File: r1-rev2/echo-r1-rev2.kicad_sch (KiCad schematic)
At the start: 100 parts, among them J1 TYPE-C-31-M-12, J2 TF-115, J6 AFC07-S30ECA-00, J7 Conn_SWDUART, J9 Micro_SD_Card, Q1 AO3401A, Q2 AO3401A, Q5 AO3401A, SW1 A, SW10 SELECT, SW11 VOL+, SW12 VOL-, SW13 POWER, SW14 HOLD, SW2 B, SW3 X, SW4 Y, SW5 DPAD↑, SW6 DPAD↓, SW7 DPAD←, SW8 DPAD→, SW9 START, U1 STM32H7R3Z8Jx, U10 USBLC6-2SC6, U11 TPAZ1143-04F, U12 TPAZ1143-04F, U13 TPAZ1143-04F, U14 TPAZ1143-04F, U2 W958D8NBYA5I, Y1 SC-32S32.768kHz20PPM12.5pF, Y2 XTM32024000JT00351001

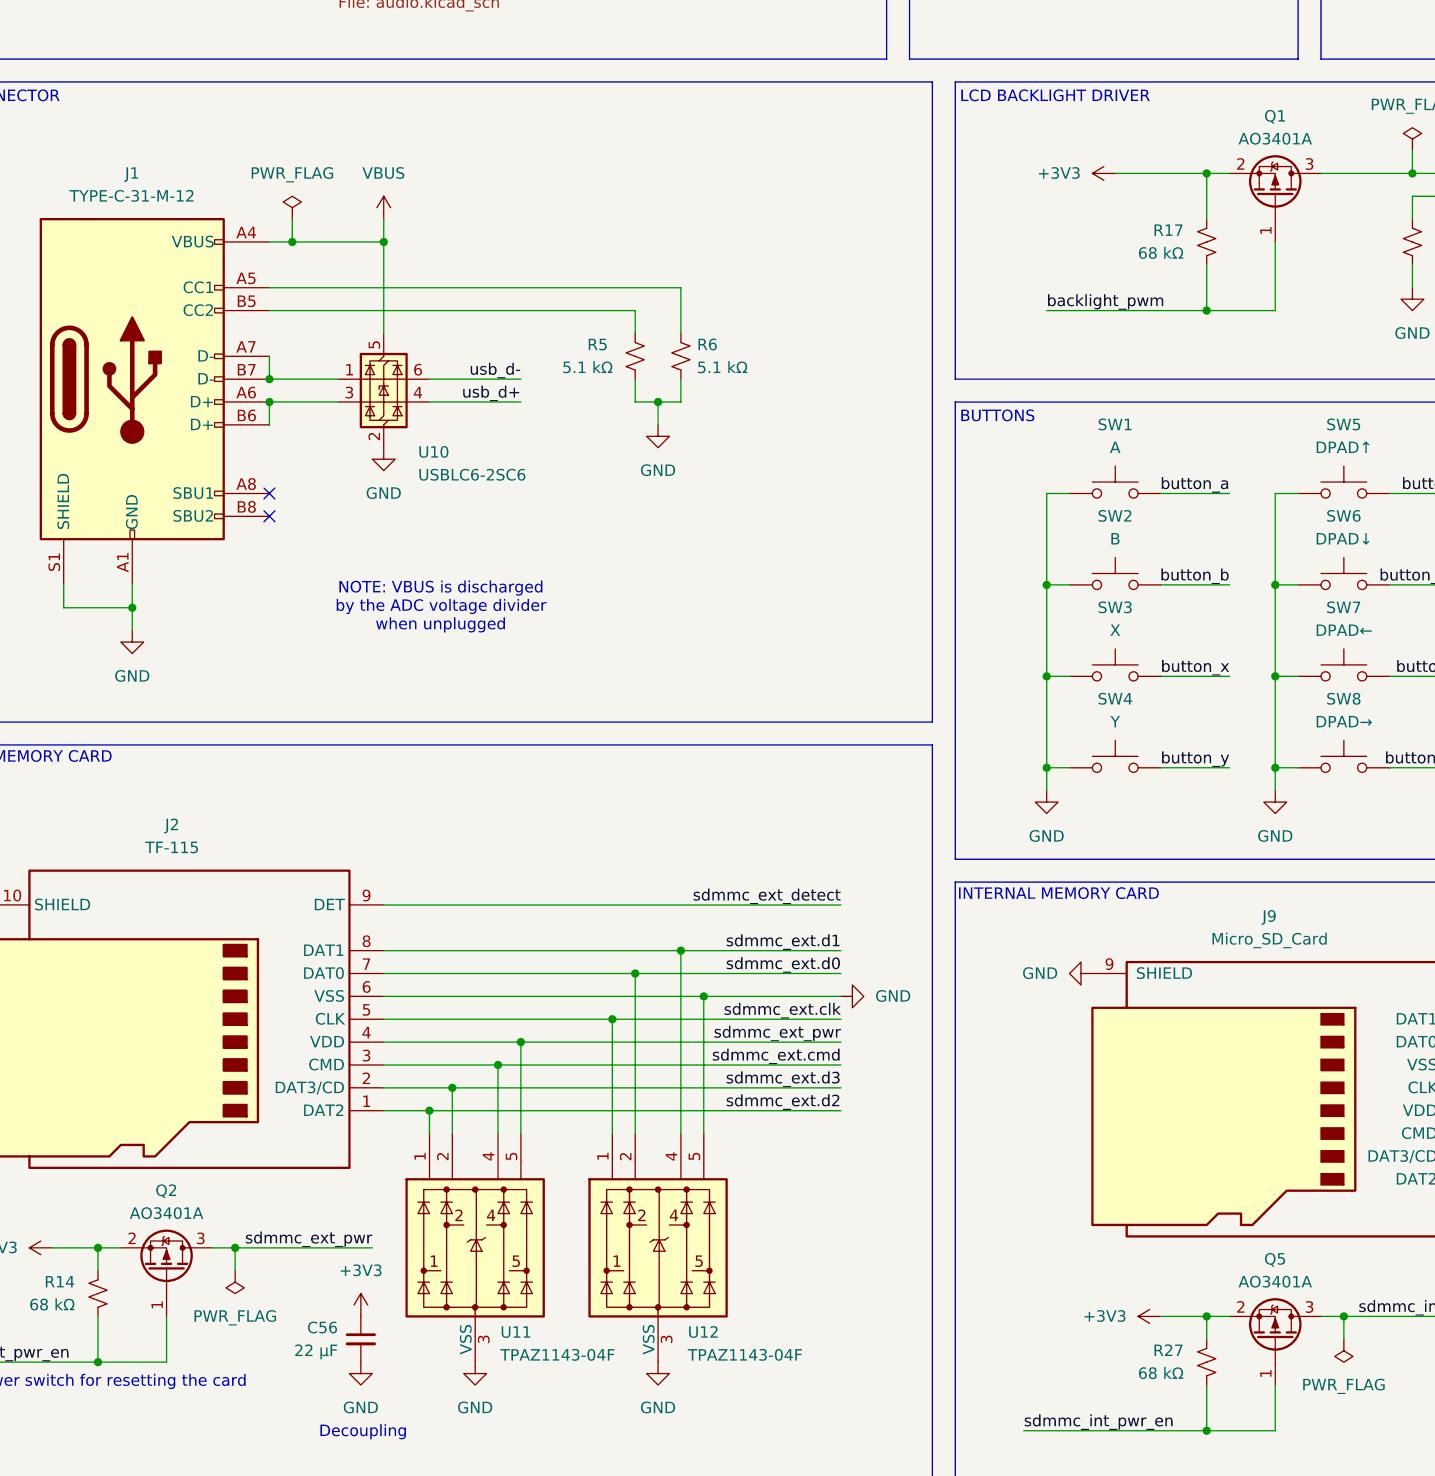
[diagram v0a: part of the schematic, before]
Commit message: Fix symbol library links & resync footprints from KiCAD libraries
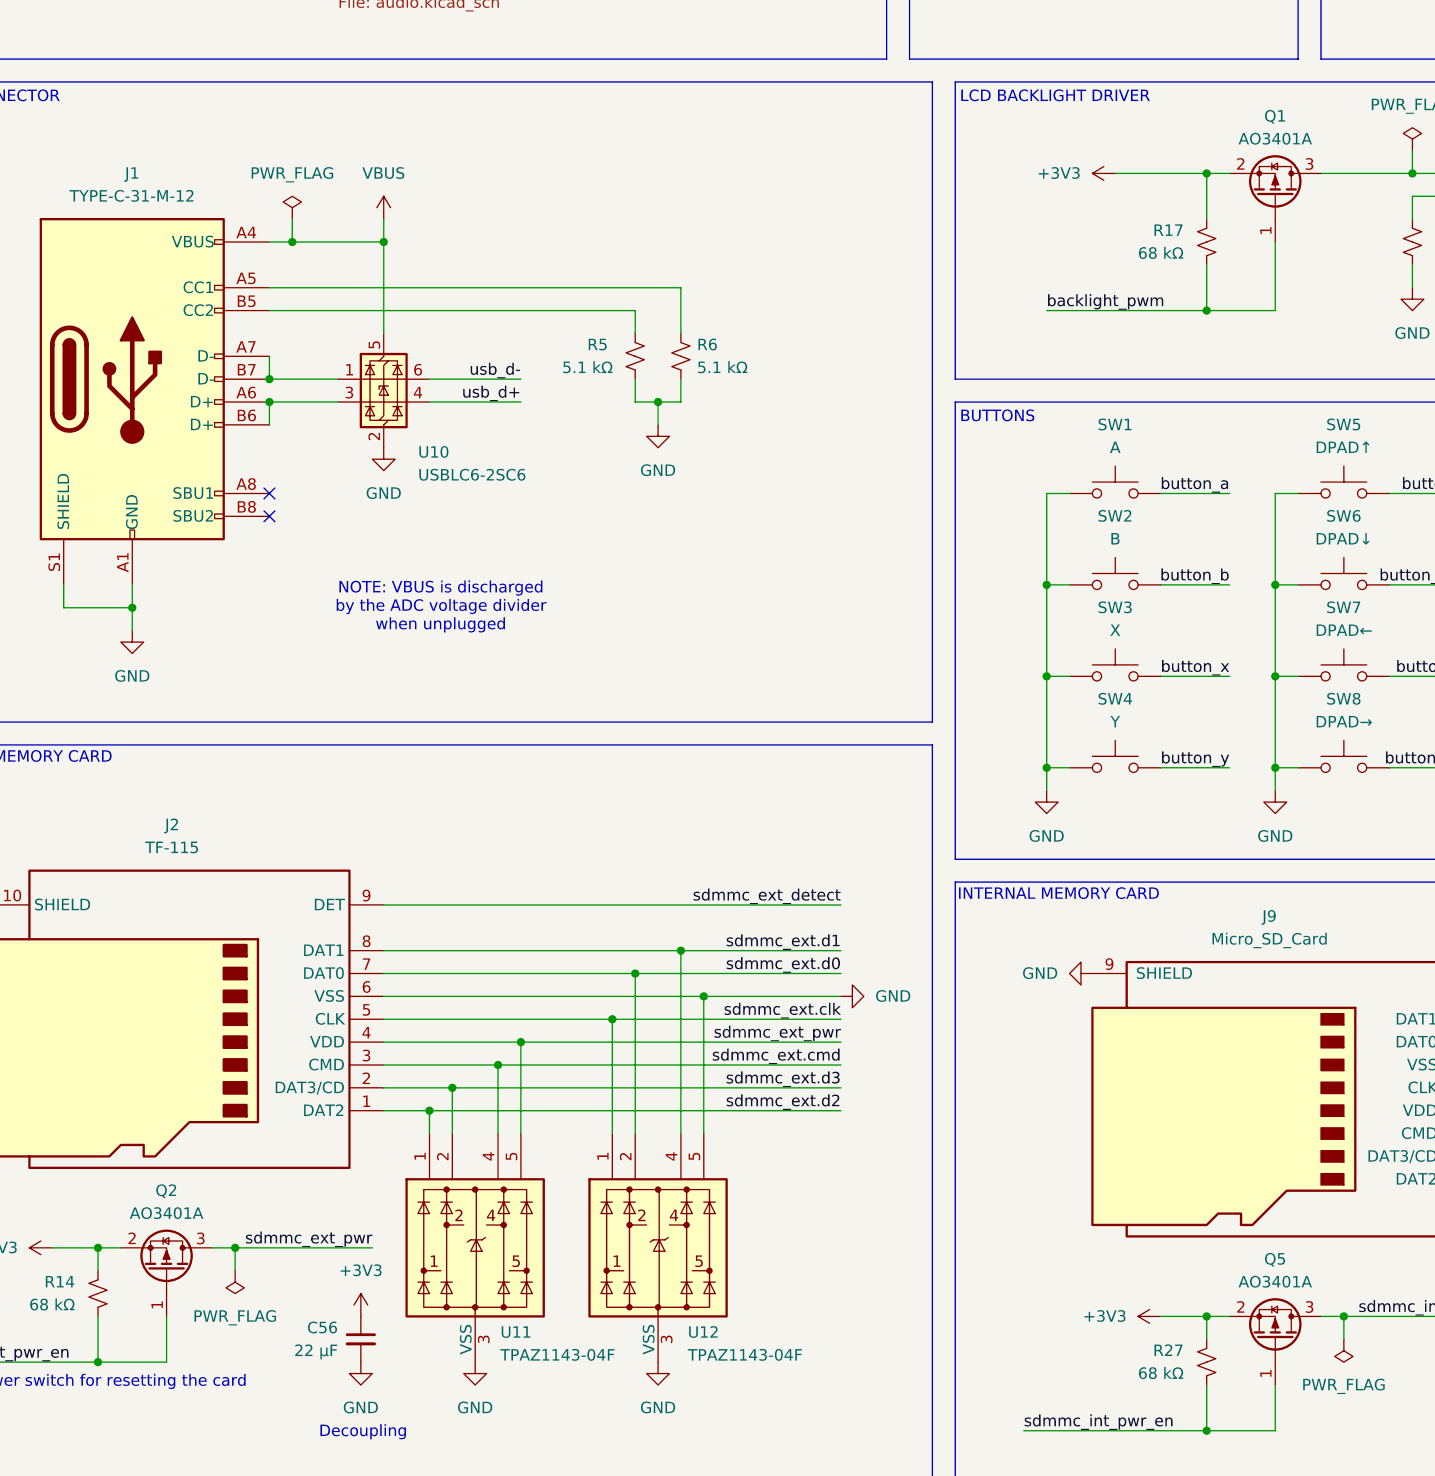
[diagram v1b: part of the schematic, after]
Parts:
- Q1, Q2, Q5: symbol Device:Q_PMOS_GSD -> Transistor_FET:Q_PMOS_GSD
